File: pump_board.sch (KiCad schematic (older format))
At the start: 6 parts

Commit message: Updated wires
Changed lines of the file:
@@
 $EndComp
 Wire Wire Line
-	5700 6100 5700 6200
-Wire Wire Line
-	5700 6200 5700 6300
-Connection ~ 5700 6200
-Wire Wire Line
-	5700 6400 5700 6300
-Connection ~ 5700 6300
-Wire Wire Line
-	6200 6200 6200 6150
+	6050 6100 6050 6050
 $Comp
 L power:+5V #PWR?
 U 1 1 5FCD4A8D
-P 6200 6150
-F 0 "#PWR?" H 6200 6000 50  0001 C CNN
-F 1 "+5V" H 6215 6323 50  0000 C CNN
-F 2 "" H 6200 6150 50  0001 C CNN
-F 3 "" H 6200 6150 50  0001 C CNN
-	1    6200 6150
+P 6050 6050
+F 0 "#PWR?" H 6050 5900 50  0001 C CNN
+F 1 "+5V" H 6065 6223 50  0000 C CNN
+F 2 "" H 6050 6050 50  0001 C CNN
+F 3 "" H 6050 6050 50  0001 C CNN
+	1    6050 6050
 	1    0    0    -1
 $EndComp
 Wire Wire Line
-	5700 6200 6200 6200
+	5700 6100 5800 6100
 Text Label 4750 6100 0    50   ~ 0
 CONN_CU1
@@
 L power:GND #PWR?
 U 1 1 5FCF66CB
-P 4000 6000
-F 0 "#PWR?" H 4000 5750 50  0001 C CNN
-F 1 "GND" H 4000 6050 50  0000 C CNN
-F 2 "" H 4000 6000 50  0001 C CNN
-F 3 "" H 4000 6000 50  0001 C CNN
-	1    4000 6000
+P 3700 6850
+F 0 "#PWR?" H 3700 6600 50  0001 C CNN
+F 1 "GND" H 3700 6700 50  0000 C CNN
+F 2 "" H 3700 6850 50  0001 C CNN
+F 3 "" H 3700 6850 50  0001 C CNN
+	1    3700 6850
 	-1   0    0    -1
 $EndComp
 Text Label 2700 6350 0    50   ~ 0
 CONN_CU3
-Wire Wire Line
-	3500 5700 3500 6000
-Connection ~ 3500 6000
-Wire Wire Line
-	3500 6000 3500 6350
-Connection ~ 3500 6350
-Wire Wire Line
-	3500 6350 3500 6700
-Wire Wire Line
-	3500 6000 4000 6000
 Wire Wire Line
 	3200 5700 2700 5700
@@
 Wire Wire Line
 	3200 6700 2700 6700
+Wire Wire Line
+	3500 5700 3700 5700
+Wire Wire Line
+	3700 5700 3700 6000
+Wire Wire Line
+	3500 6000 3700 6000
+Connection ~ 3700 6000
+Wire Wire Line
+	3700 6000 3700 6350
+Wire Wire Line
+	3500 6350 3700 6350
+Connection ~ 3700 6350
+Wire Wire Line
+	3500 6700 3700 6700
+Wire Wire Line
+	3700 6350 3700 6700
+Connection ~ 3700 6700
+Wire Wire Line
+	3700 6700 3700 6850
+Wire Wire Line
+	5800 6100 5800 6200
+Wire Wire Line
+	5800 6200 5700 6200
+Wire Wire Line
+	5800 6200 5800 6300
+Wire Wire Line
+	5800 6300 5700 6300
+Connection ~ 5800 6200
+Wire Wire Line
+	5800 6300 5800 6400
+Wire Wire Line
+	5800 6400 5700 6400
+Connection ~ 5800 6300
+Wire Wire Line
+	5800 6100 6050 6100
+Connection ~ 5800 6100
 $EndSCHEMATC

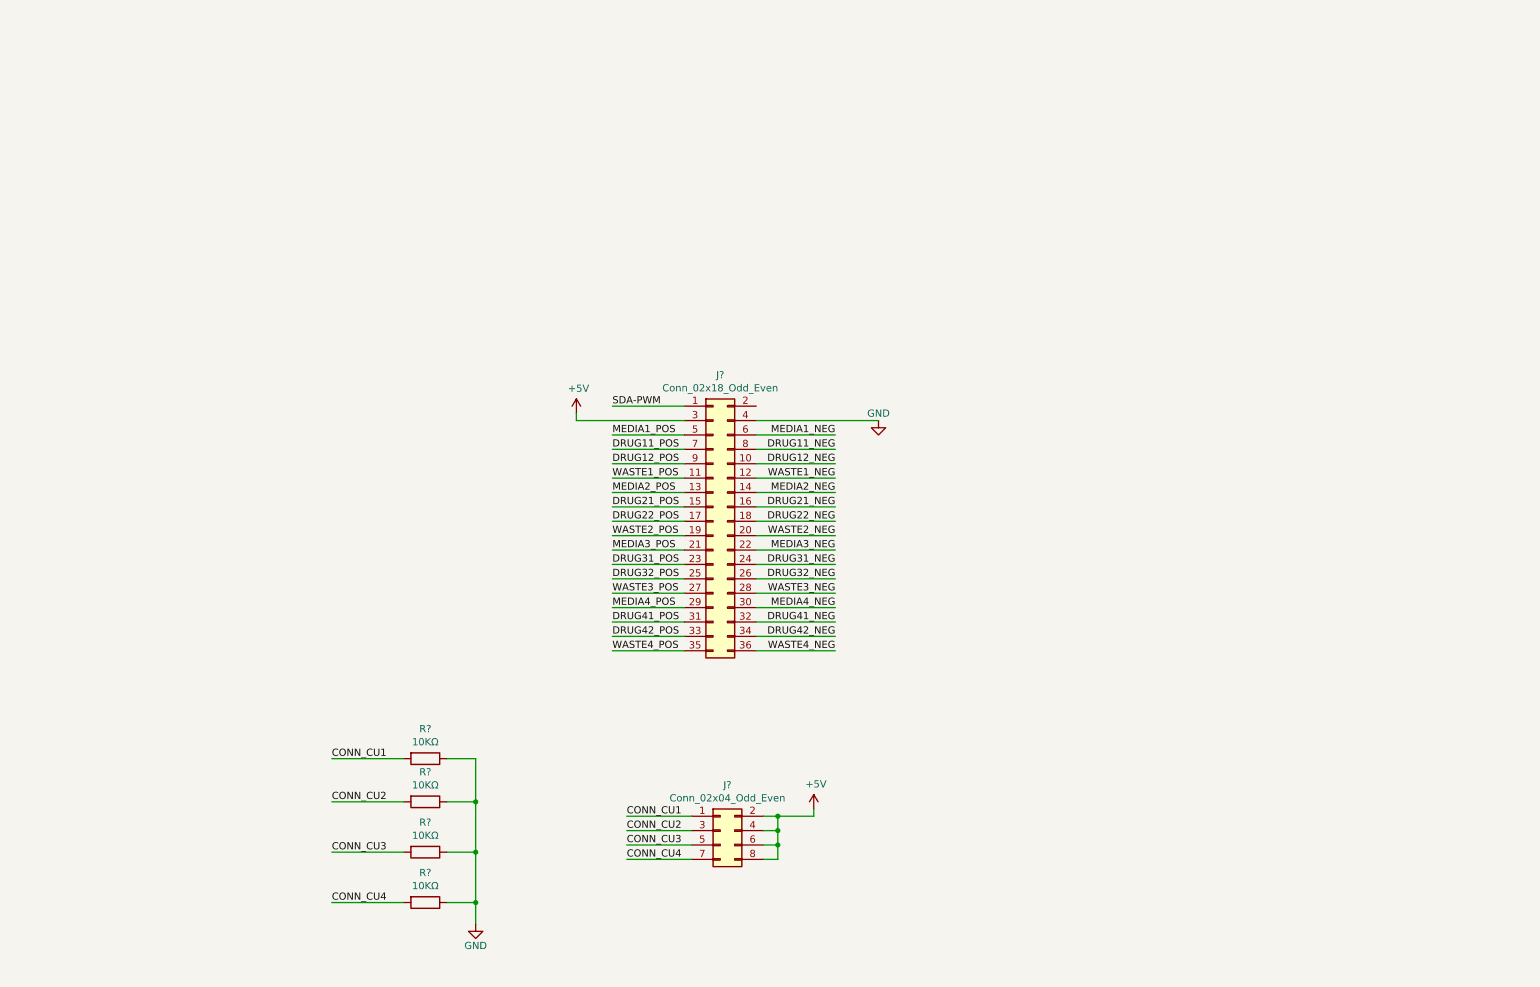
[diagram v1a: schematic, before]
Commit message: Added transistors
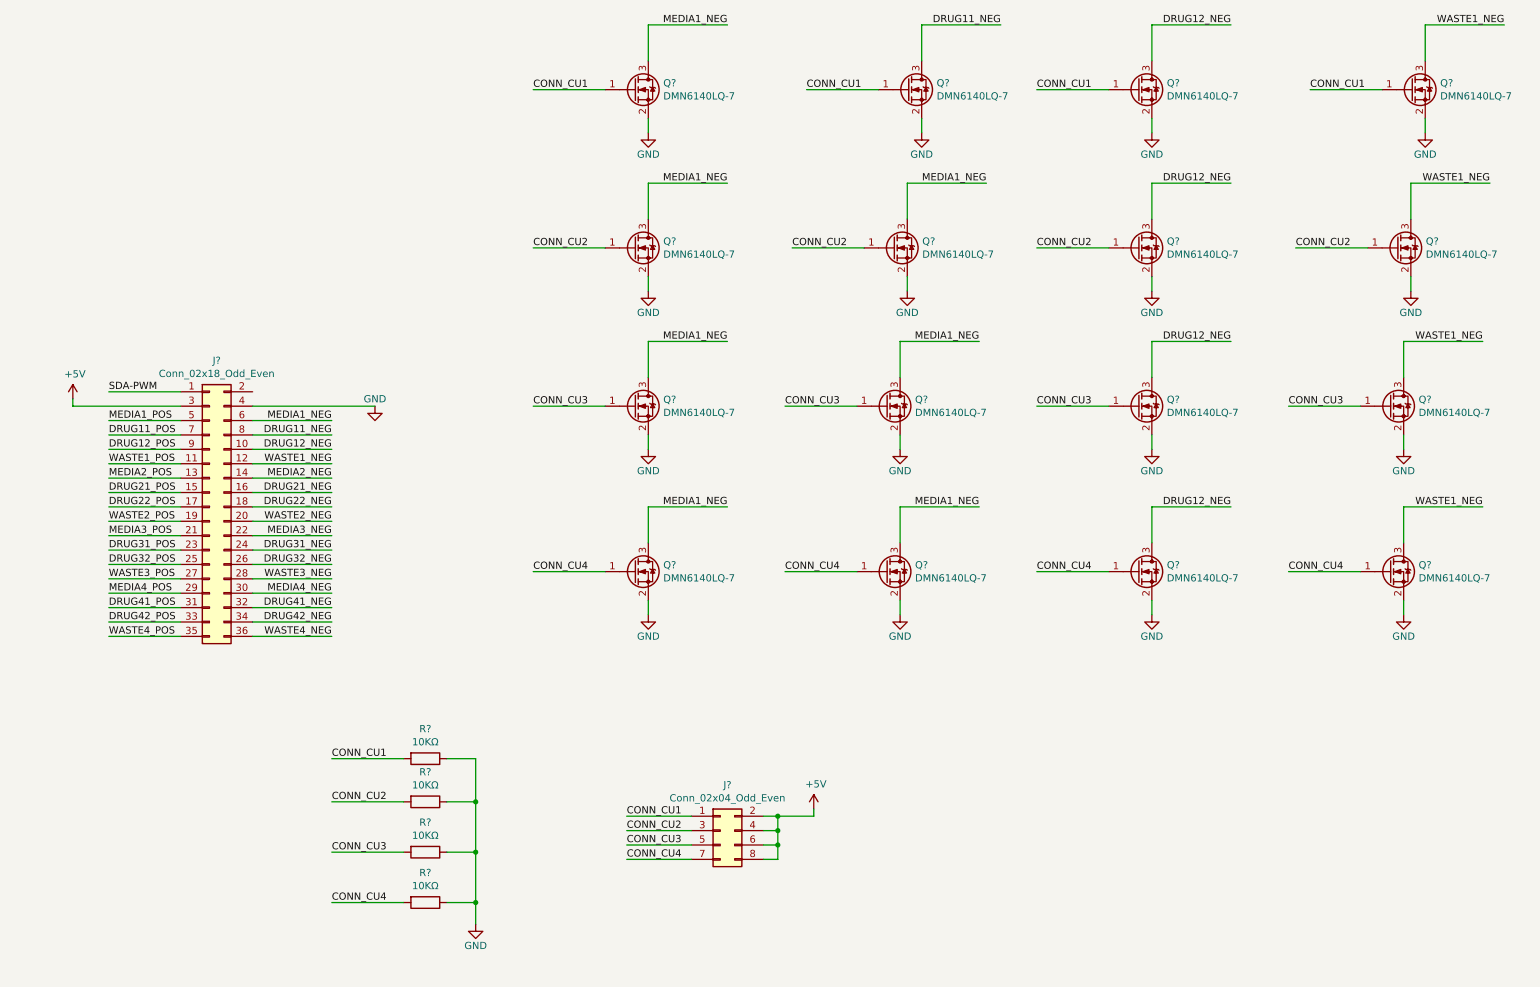
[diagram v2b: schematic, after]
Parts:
- added Q? (x16): DMN6140LQ-7, Package_TO_SOT_SMD:SOT-23, symbol Transistor_FET:DMN10H220L
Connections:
- net CONN_CU1: now also Q?.1 (G), Q?.1 (G), Q?.1 (G), Q?.1 (G)
- net CONN_CU2: now also Q?.1 (G), Q?.1 (G), Q?.1 (G), Q?.1 (G)
- net CONN_CU3: now also Q?.1 (G), Q?.1 (G), Q?.1 (G), Q?.1 (G)
- net CONN_CU4: now also Q?.1 (G), Q?.1 (G), Q?.1 (G), Q?.1 (G)
- net DRUG11_NEG: now also Q?.3 (D)
- net DRUG12_NEG: now also Q?.3 (D), Q?.3 (D), Q?.3 (D), Q?.3 (D)
- net GND: now also Q?.2 (S), Q?.2 (S), Q?.2 (S), Q?.2 (S), Q?.2 (S), Q?.2 (S), Q?.2 (S), Q?.2 (S), Q?.2 (S), Q?.2 (S), Q?.2 (S), Q?.2 (S), Q?.2 (S), Q?.2 (S), Q?.2 (S), Q?.2 (S)
- net MEDIA1_NEG: now also Q?.3 (D), Q?.3 (D), Q?.3 (D), Q?.3 (D), Q?.3 (D), Q?.3 (D), Q?.3 (D)
- net WASTE1_NEG: now also Q?.3 (D), Q?.3 (D), Q?.3 (D), Q?.3 (D)
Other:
- moved on the sheet: J?

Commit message: added connections
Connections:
- net DRUG21_NEG is gone; now on net DRUG11_NEG: J?.16 (Pin_16)
- net DRUG21_POS is gone; now on net DRUG11_POS: J?.15 (Pin_15)
- net DRUG22_NEG is gone; now on net DRUG12_NEG: J?.18 (Pin_18)
- net DRUG22_POS is gone; now on net DRUG12_POS: J?.17 (Pin_17)
- net DRUG31_NEG is gone; now on net DRUG11_NEG: J?.24 (Pin_24)
- net DRUG31_POS is gone; now on net DRUG11_POS: J?.23 (Pin_23)
- net DRUG32_NEG is gone; now on net DRUG12_NEG: J?.26 (Pin_26)
- net DRUG32_POS is gone; now on net DRUG12_POS: J?.25 (Pin_25)
- net DRUG41_NEG is gone; now on net DRUG11_NEG: J?.32 (Pin_32)
- net DRUG41_POS is gone; now on net DRUG11_POS: J?.31 (Pin_31)
- net DRUG42_NEG is gone; now on net DRUG12_NEG: J?.34 (Pin_34)
- net DRUG42_POS is gone; now on net DRUG12_POS: J?.33 (Pin_33)
- net MEDIA2_NEG is gone; now on net MEDIA1_NEG: J?.14 (Pin_14)
- net MEDIA2_POS is gone; now on net MEDIA1_POS: J?.13 (Pin_13)
- net MEDIA3_NEG is gone; now on net MEDIA1_NEG: J?.22 (Pin_22)
- net MEDIA3_POS is gone; now on net MEDIA1_POS: J?.21 (Pin_21)
- net MEDIA4_NEG is gone; now on net MEDIA1_NEG: J?.30 (Pin_30)
- net MEDIA4_POS is gone; now on net MEDIA1_POS: J?.29 (Pin_29)
- net WASTE2_NEG is gone; now on net WASTE1_NEG: J?.20 (Pin_20)
- net WASTE2_POS is gone; now on net WASTE1_POS: J?.19 (Pin_19)
- net WASTE3_NEG is gone; now on net WASTE1_NEG: J?.28 (Pin_28)
- net WASTE3_POS is gone; now on net WASTE1_POS: J?.27 (Pin_27)
- net WASTE4_NEG is gone; now on net WASTE1_NEG: J?.36 (Pin_36)
- net WASTE4_POS is gone; now on net WASTE1_POS: J?.35 (Pin_35)
- net DRUG11_NEG: now also Q?.3 (D), Q?.3 (D), Q?.3 (D)
- net MEDIA1_NEG: no longer Q?.3 (D), Q?.3 (D), Q?.3 (D)
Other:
- moved on the sheet: J?
